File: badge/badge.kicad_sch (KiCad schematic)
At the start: 6 parts, among them U1 TPS7250QP

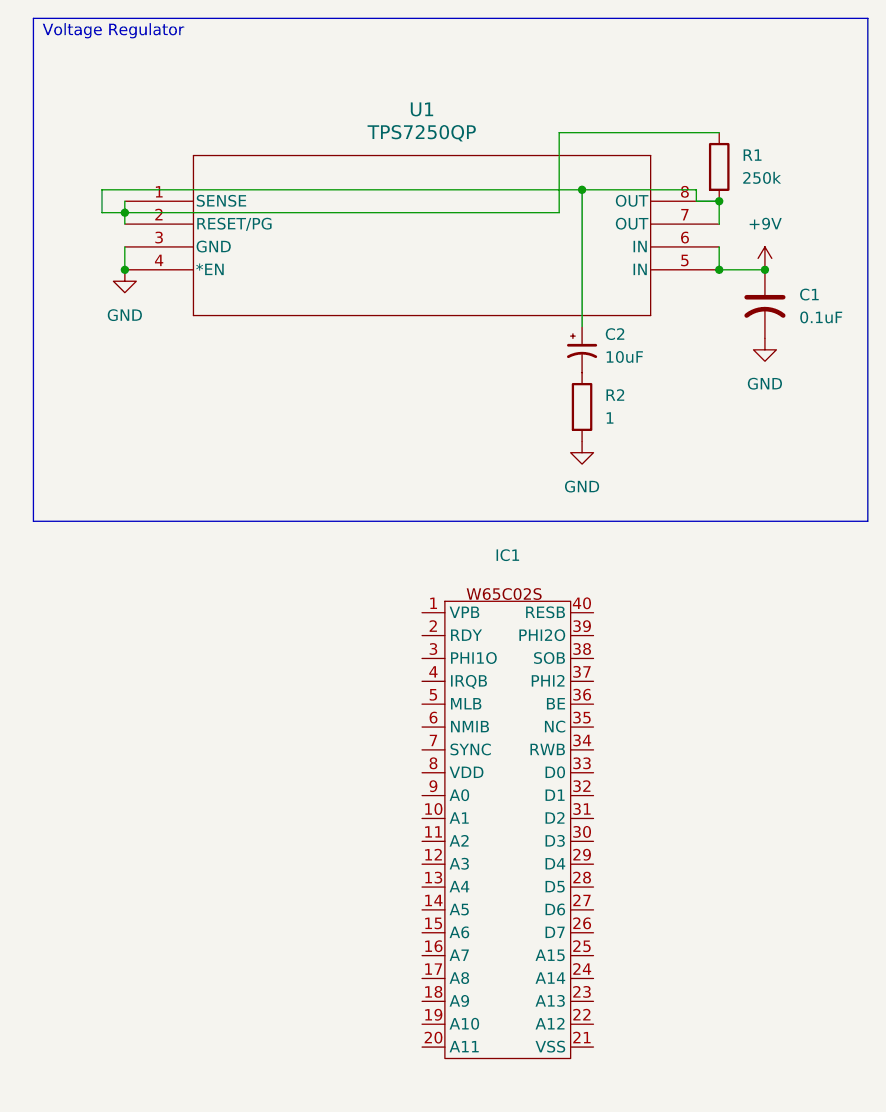
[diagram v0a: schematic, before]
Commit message: Add core 6502 Wiring
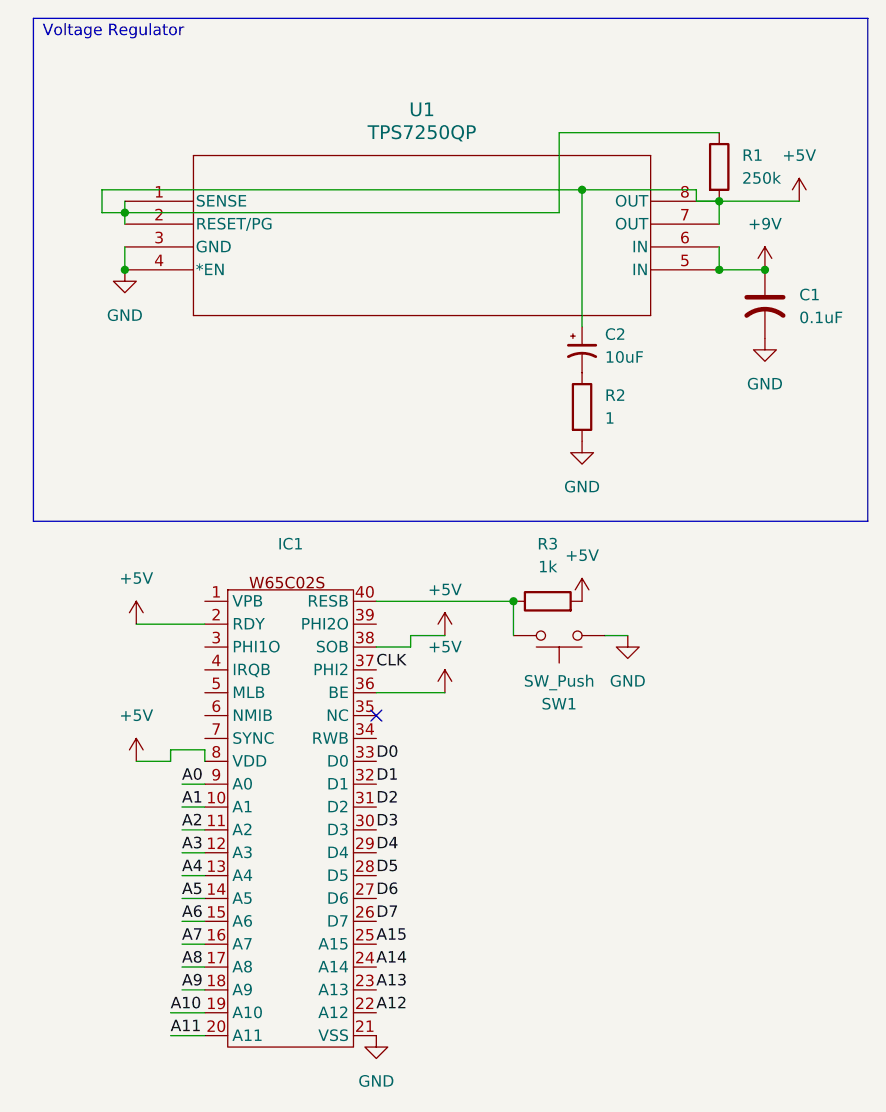
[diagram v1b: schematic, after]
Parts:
- added R3: 1k, symbol Device:R
- added SW1: SW_Push, symbol Switch:SW_Push
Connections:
- net GND: now also IC1.21 (VSS), SW1.2
- net +5V: now reaches C2.1, R1.1, R1.2, U1.1 (SENSE), U1.2 (RESET/PG), U1.7 (OUT), U1.8 (OUT)
- net +5V: now also IC1.2 (RDY), IC1.36 (BE), IC1.38 (SOB), IC1.8 (VDD), R3.2
- net A1: now reaches IC1.10 (A1)
- net A2: now reaches IC1.11 (A2)
- net A3: now reaches IC1.12 (A3)
- net A4: now reaches IC1.13 (A4)
- net A5: now reaches IC1.14 (A5)
- net A6: now reaches IC1.15 (A6)
- net A7: now reaches IC1.16 (A7)
- net A8: now reaches IC1.17 (A8)
- net A9: now reaches IC1.18 (A9)
- net A10: now reaches IC1.19 (A10)
- net A11: now reaches IC1.20 (A11)
- net A12: now reaches IC1.22 (A12)
- net A13: now reaches IC1.23 (A13)
- net A14: now reaches IC1.24 (A14)
- net A15: now reaches IC1.25 (A15)
- net D7: now reaches IC1.26 (D7)
- net D6: now reaches IC1.27 (D6)
- net D5: now reaches IC1.28 (D5)
- net D4: now reaches IC1.29 (D4)
- net D3: now reaches IC1.30 (D3)
- net D2: now reaches IC1.31 (D2)
- net D1: now reaches IC1.32 (D1)
- net D0: now reaches IC1.33 (D0)
- net CLK: now reaches IC1.37 (PHI2)
- net at IC1.40 (RESB): now also R3.1, SW1.1
- net A0: now reaches IC1.9 (A0)
- no-connect marks 0 -> 1
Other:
- moved on the sheet: IC1

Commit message: Make the voltage regulator look nice
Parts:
- removed U1: TPS7250QP, P8_TEX, symbol TPS7250QP:TPS7250QP
- added U2: ~, symbol 6502ConferenceBadge:TPS7250QP
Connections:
- net +5V: now also U2.1 (SENSE), U2.7 (OUT), U2.8 (OUT); no longer R1.1
- net +9V: now also U2.5 (IN), U2.6 (IN)
- net GND: now also U2.3 (GND), U2.4 (EN)
- new net: R1.1, U2.2 (PG)
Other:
- note added: "W65C02S / CPU"
- moved on the sheet: IC1, R3, SW1

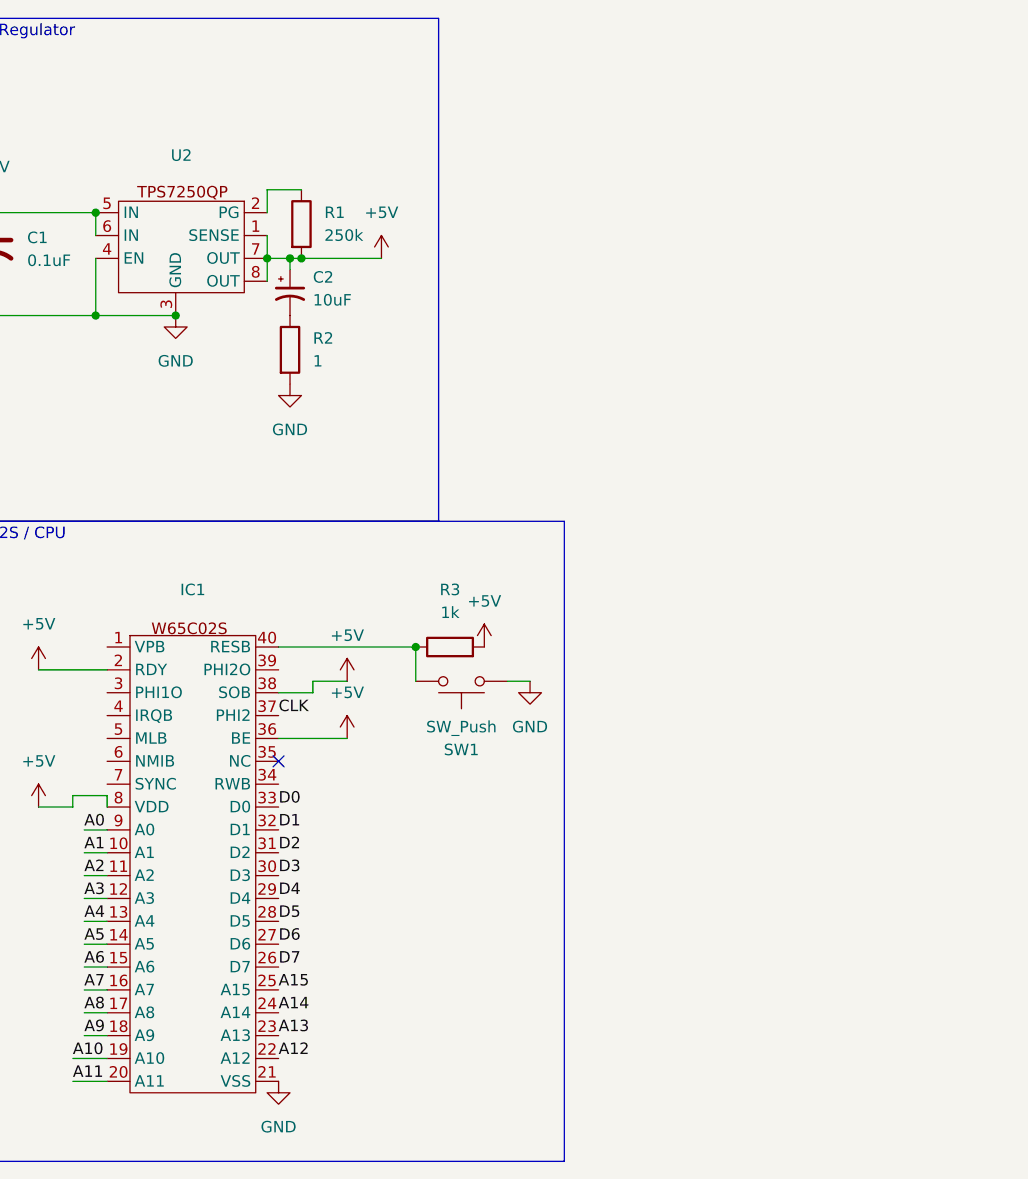
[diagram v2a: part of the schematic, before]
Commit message: Add ROM
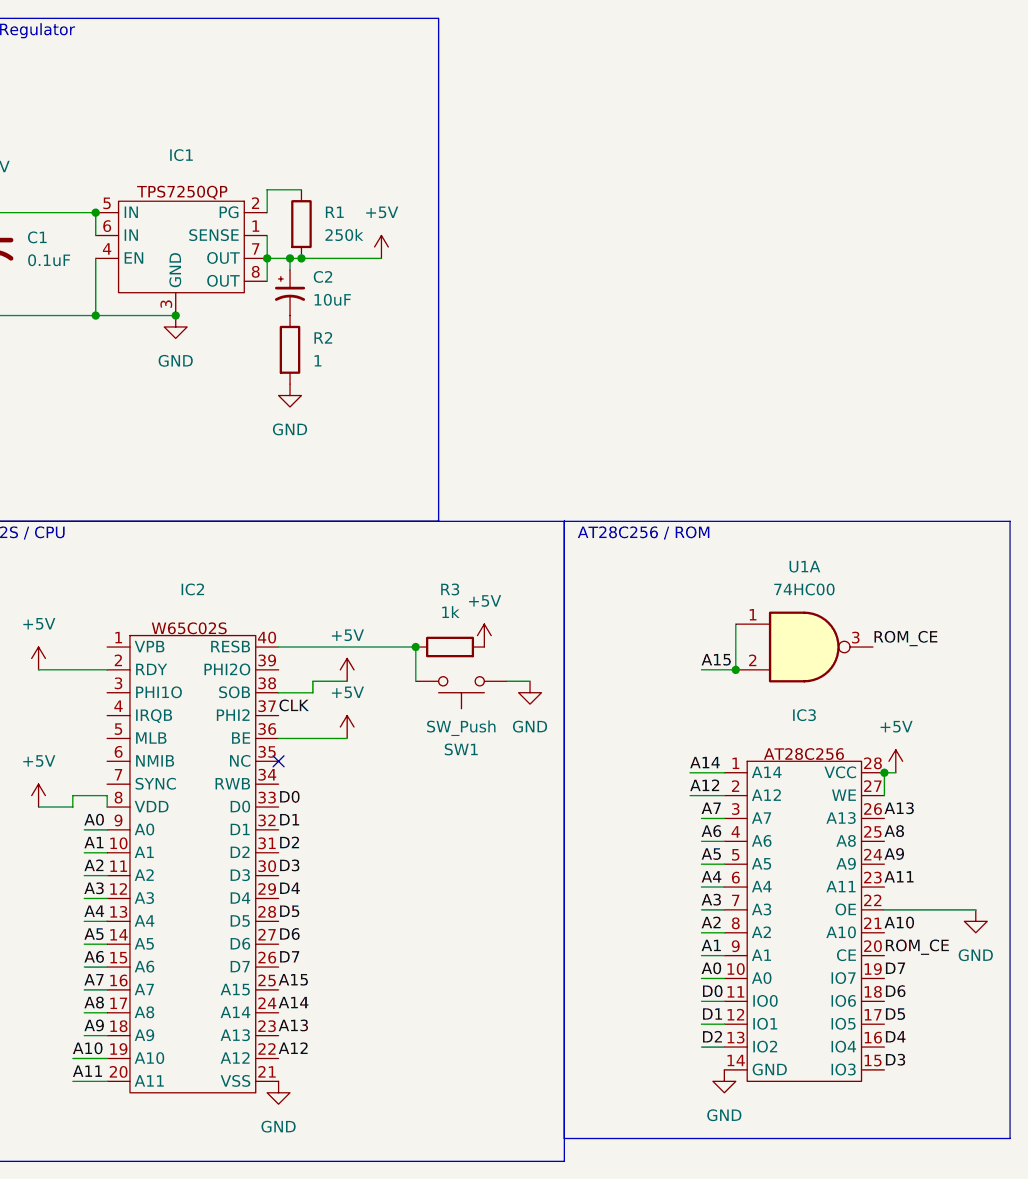
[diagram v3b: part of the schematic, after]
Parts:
- added IC3: ~, symbol 6502ConferenceBadge:AT28C256
- added U1: 74HC00, symbol 74xx:74HC00
- renumbered U2 to IC1, IC1 to IC2
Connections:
- net +5V: now also IC3.27 (WE), IC3.28 (VCC)
- net A0: now also IC3.10 (A0)
- net A1: now also IC3.9 (A1)
- net A10: now also IC3.21 (A10)
- net A11: now also IC3.23 (A11)
- net A12: now also IC3.2 (A12)
- net A13: now also IC3.26 (A13)
- net A14: now also IC3.1 (A14)
- net A15: now also U1.1, U1.2
- net A2: now also IC3.8 (A2)
- net A3: now also IC3.7 (A3)
- net A4: now also IC3.6 (A4)
- net A5: now also IC3.5 (A5)
- net A6: now also IC3.4 (A6)
- net A7: now also IC3.3 (A7)
- net A8: now also IC3.25 (A8)
- net A9: now also IC3.24 (A9)
- net D0: now also IC3.11 (IO0)
- net D1: now also IC3.12 (IO1)
- net D2: now also IC3.13 (IO2)
- net D3: now also IC3.15 (IO3)
- net D4: now also IC3.16 (IO4)
- net D5: now also IC3.17 (IO5)
- net D6: now also IC3.18 (IO6)
- net D7: now also IC3.19 (IO7)
- net GND: now also IC3.14 (GND), IC3.22 (OE)
- new net ROM_CE: IC3.20 (CE), U1.3
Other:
- note added: "AT28C256 / ROM"
- company: (none) -> Sean Outram
- title: (none) -> 6502 Conference Badge

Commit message: VIA design work and Progress Check
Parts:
- added IC4: ~, symbol 6502ConferenceBadge:W65C22
- added unit 2 of U1
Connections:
- net +5V: now also IC4.1 (VSS)
- net A0: now also IC4.38 (RS0)
- net A1: now also IC4.37 (RS1)
- net A13: now also IC4.24 (CS1)
- net A14: now also U1.5
- net A2: now also IC4.36 (RS2)
- net A3: now also IC4.35 (RS3)
- net CLK: now also IC4.25 (PHI2)
- net D0: now also IC4.33 (D0)
- net D1: now also IC4.32 (D1)
- net D2: now also IC4.31 (D2)
- net D3: now also IC4.30 (D3)
- net D4: now also IC4.29 (D4)
- net D5: now also IC4.28 (D5)
- net D6: now also IC4.27 (D6)
- net D7: now also IC4.26 (D7)
- net GND: now also IC4.20 (VDD)
- net ROM_CE: now also U1.4
- net RST: now reaches IC2.40 (RESB), R3.1, SW1.1
- net RST: now also IC4.34 (RESB)
- net RW: now reaches IC2.34 (RWB)
- net RW: now also IC4.22 (RWB)
- new net VIA_CS2: IC4.23 (CS2B), U1.6
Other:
- note added: "WC65C22 / VIA"
- note added: "We can reuse the NAND gate already on A15"
- moved on the sheet: IC3, U1A

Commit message: Output LEDS
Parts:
- added D1, D2, D3, D4, D5, D6, D7, D8: RED, symbol Device:LED
- added RN1: 220, bussed, Resistor_THT:R_Array_SIP9, symbol Device:R_Network08
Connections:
- net GND: now also RN1.1 (common)
- net PB0: now reaches IC4.10 (PB0)
- net PB0: now also D1.2 (A)
- net PB1: now reaches IC4.11 (PB1)
- net PB1: now also D2.2 (A)
- net PB2: now reaches IC4.12 (PB2)
- net PB2: now also D3.2 (A)
- net PB3: now reaches IC4.13 (PB3)
- net PB3: now also D4.2 (A)
- net PB4: now reaches IC4.14 (PB4)
- net PB4: now also D5.2 (A)
- net PB5: now reaches IC4.15 (PB5)
- net PB5: now also D6.2 (A)
- net PB6: now reaches IC4.16 (PB6)
- net PB6: now also D7.2 (A)
- net PB7: now reaches IC4.17 (PB7)
- net PB7: now also D8.2 (A)
- new net: D8.1 (K), RN1.9 (R8)
- new net: D1.1 (K), RN1.2 (R1)
- new net: D2.1 (K), RN1.3 (R2)
- new net: D3.1 (K), RN1.4 (R3)
- new net: D4.1 (K), RN1.5 (R4)
- new net: D5.1 (K), RN1.6 (R5)
- new net: D6.1 (K), RN1.7 (R6)
- new net: D7.1 (K), RN1.8 (R7)
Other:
- note added: "OUTPUT LEDS"

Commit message: Partially add RAM, and a fair amount of commentry about desires with the design
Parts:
- added IC5: ~, symbol 6502ConferenceBadge:AS6C62256
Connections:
- net +5V: now also IC4.20 (VDD), IC5.28 (VCC); no longer IC4.1 (VSS)
- net A0: now also IC5.10 (A0)
- net A1: now also IC5.9 (A1)
- net A10: now also IC5.21 (A10)
- net A11: now also IC5.23 (A11)
- net A12: now also IC5.2 (A12)
- net A13: now also IC5.26 (A13)
- net A14: now also IC5.1 (A14)
- net A2: now also IC5.8 (A2)
- net A3: now also IC5.7 (A3)
- net A4: now also IC5.6 (A4)
- net A5: now also IC5.5 (A5)
- net A6: now also IC5.4 (A6)
- net A7: now also IC5.3 (A7)
- net A8: now also IC5.25 (A8)
- net A9: now also IC5.24 (A9)
- net D3: now also IC5.15 (DQ3)
- net D4: now also IC5.16 (DQ4)
- net D5: now also IC5.17 (DQ5)
- net D6: now also IC5.18 (DQ6)
- net D7: now also IC5.19 (DQ7)
- net GND: now also IC4.1 (VSS), IC5.14 (VSS); no longer IC4.20 (VDD)
- net RW: now also IC5.27 (WE#)

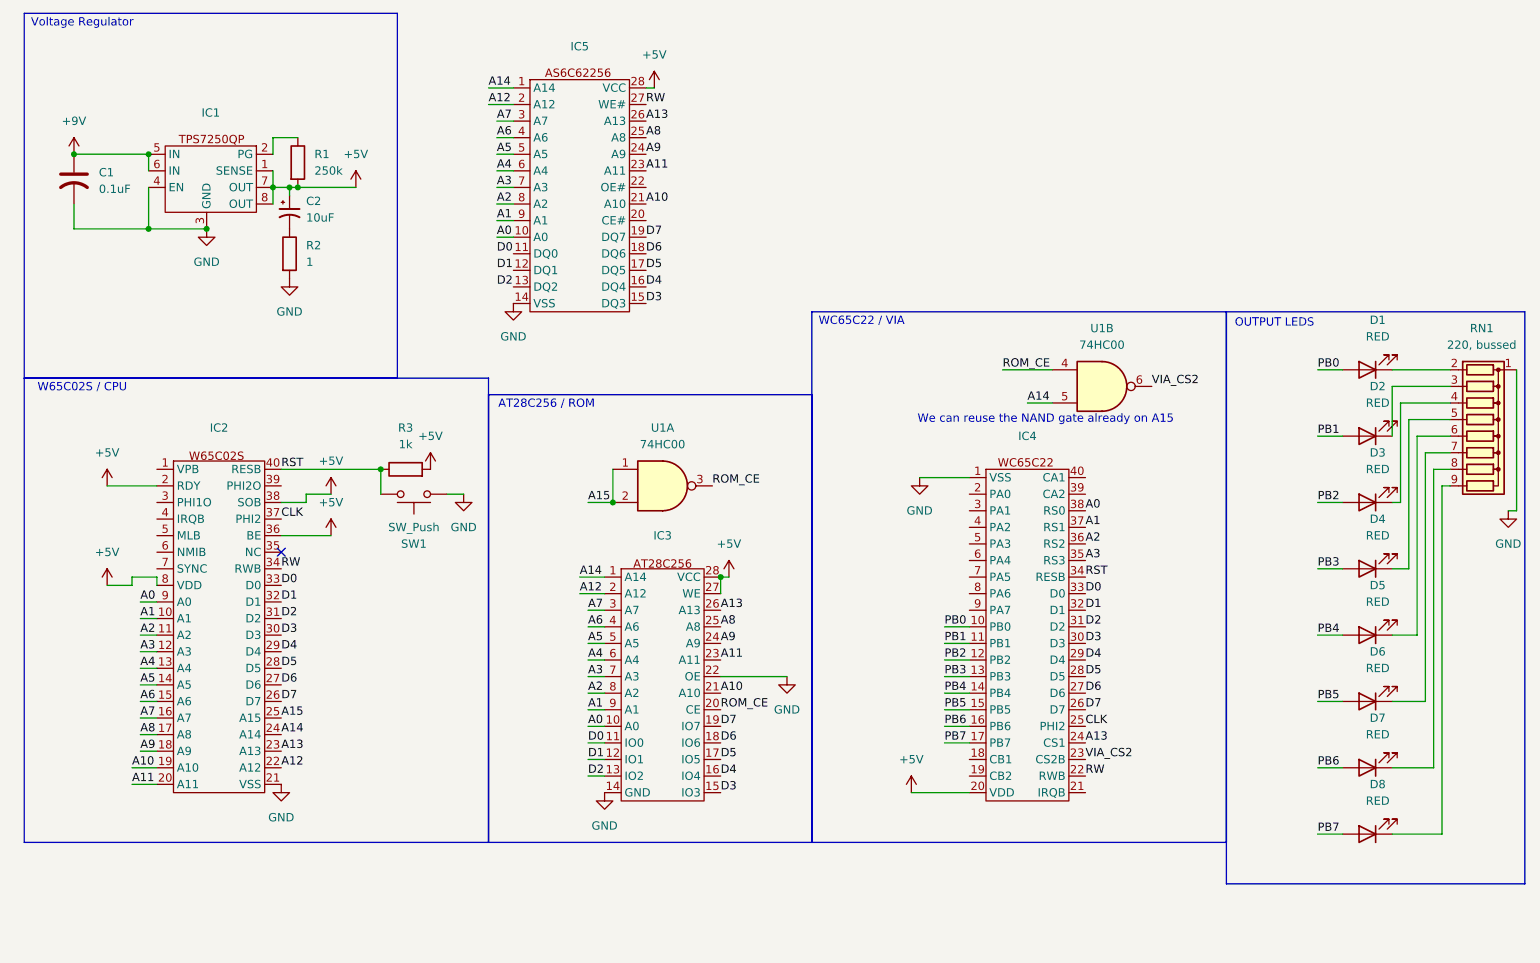
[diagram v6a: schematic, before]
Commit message: Add the Address Decoding PLD
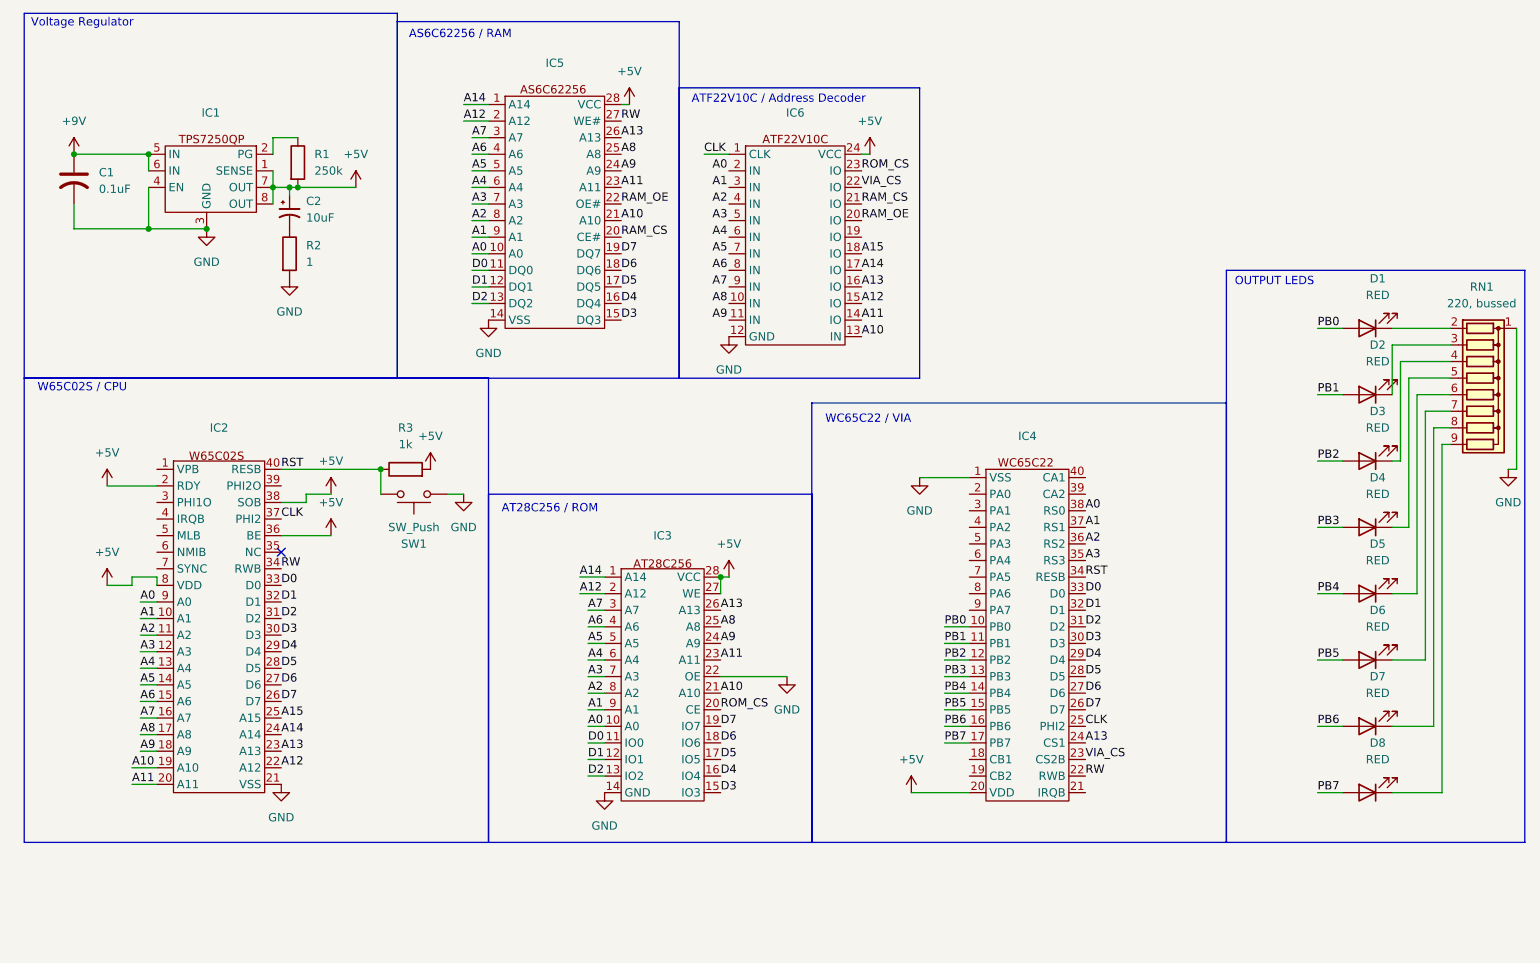
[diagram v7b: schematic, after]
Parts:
- removed U1: 74HC00, symbol 74xx:74HC00
- added IC6: ~, symbol 6502ConferenceBadge:ATF22V10C
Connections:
- net +5V: now also IC6.24 (VCC)
- net A10: now also IC6.13 (IN)
- net A11: now also IC6.14 (IO)
- net A12: now also IC6.15 (IO)
- net A13: now also IC6.16 (IO)
- net A14: now also IC6.17 (IO)
- net A15: now also IC6.18 (IO)
- net CLK: now also IC6.1 (CLK)
- net D0: now also IC5.11 (DQ0)
- net D1: now also IC5.12 (DQ1)
- net D2: now also IC5.13 (DQ2)
- net GND: now also IC6.12 (GND)
- net RAM_CS: now reaches IC5.20 (CE#)
- net RAM_CS: now also IC6.21 (IO)
- net RAM_OE: now reaches IC5.22 (OE#)
- net RAM_OE: now also IC6.20 (IO)
- net ROM_CE renamed ROM_CS
- net ROM_CS: now also IC6.23 (IO)
- net VIA_CS2 renamed VIA_CS
- net VIA_CS: now also IC6.22 (IO)
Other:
- note added: "AS6C62256 / RAM"
- note added: "ATF22V10C / Address Decoder"
- note removed: "We can reuse the NAND gate already on A15"
- moved on the sheet: D1, D2, D3, D4, D5, D6, D7, D8, IC5, RN1
